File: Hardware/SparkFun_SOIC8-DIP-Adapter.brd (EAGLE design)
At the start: 20.3 x 20.3 mm, 17 parts, among them U1 GENERIC-SOIC8, U2 GENERIC-SOIC8, U3 GENERIC-SOIC8, U4 GENERIC-SOIC8

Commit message: Some small updates
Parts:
- FRAME1: value (none) -> frame
- JP1, JP2, JP3, JP4, JP5, JP6, JP7, JP8: value (none) -> 1x4
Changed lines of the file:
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@@
 <layer number="49" name="Reference" color="7" fill="1" visible="no" active="yes"/>
 <layer number="50" name="dxf" color="7" fill="1" visible="no" active="no"/>
-<layer number="51" name="tDocu" color="6" fill="1" visible="no" active="yes"/>
+<layer number="51" name="tDocu" color="6" fill="1" visible="yes" active="yes"/>
 <layer number="52" name="bDocu" color="7" fill="1" visible="no" active="yes"/>
 <layer number="53" name="tGND_GNDA" color="7" fill="9" visible="no" active="no"/>
@@
 <text x="19.558" y="-7.62" size="1.9304" layer="51" font="vector">Byron Jacquot</text>
 <text x="7.112" y="10.414" size="0.8128" layer="16" font="vector" ratio="25" rot="MR0">V11</text>
+<circle x="7.874" y="17.526" radius="0.127" width="0.254" layer="21"/>
+<circle x="18.034" y="17.526" radius="0.127" width="0.254" layer="21"/>
+<circle x="18.034" y="7.366" radius="0.127" width="0.254" layer="21"/>
+<circle x="7.874" y="7.366" radius="0.127" width="0.254" layer="21"/>
 </plain>
 <attributes>
@@
 </autorouter>
 <elements>
-<element name="FRAME1" library="SparkFun-Aesthetics" package="CREATIVE_COMMONS" value="" x="-11.43" y="-7.62">
+<element name="FRAME1" library="SparkFun-Aesthetics" package="CREATIVE_COMMONS" value="frame" x="-11.43" y="-7.62">
 <attribute name="VERSION" value="v01" x="-11.43" y="-7.62" size="1.778" layer="27" display="off"/>
 <attribute name="DESIGNER" value="NAME" x="-11.43" y="-7.62" size="1.778" layer="27" display="off"/>
 </element>
-<element name="JP1" library="SparkFun-Connectors" package="1X04_NO_SILK_ALL_ROUND" value="" x="1.27" y="19.05" rot="R270"/>
-<element name="JP2" library="SparkFun-Connectors" package="1X04_NO_SILK_ALL_ROUND" value="" x="8.89" y="19.05" rot="R270"/>
-<element name="JP3" library="SparkFun-Connectors" package="1X04_NO_SILK_ALL_ROUND" value="" x="11.43" y="19.05" rot="R270"/>
-<element name="JP4" library="SparkFun-Connectors" package="1X04_NO_SILK_ALL_ROUND" value="" x="19.05" y="19.05" rot="R270"/>
-<element name="JP5" library="SparkFun-Connectors" package="1X04_NO_SILK_ALL_ROUND" value="" x="1.27" y="8.89" rot="R270"/>
-<element name="JP6" library="SparkFun-Connectors" package="1X04_NO_SILK_ALL_ROUND" value="" x="8.89" y="8.89" rot="R270"/>
-<element name="JP7" library="SparkFun-Connectors" package="1X04_NO_SILK_ALL_ROUND" value="" x="11.43" y="8.89" rot="R270"/>
-<element name="JP8" library="SparkFun-Connectors" package="1X04_NO_SILK_ALL_ROUND" value="" x="19.05" y="8.89" rot="R270"/>
+<element name="JP1" library="SparkFun-Connectors" package="1X04_NO_SILK_ALL_ROUND" value="1x4" x="1.27" y="19.05" rot="R270"/>
+<element name="JP2" library="SparkFun-Connectors" package="1X04_NO_SILK_ALL_ROUND" value="1x4" x="8.89" y="19.05" rot="R270"/>
+<element name="JP3" library="SparkFun-Connectors" package="1X04_NO_SILK_ALL_ROUND" value="1x4" x="11.43" y="19.05" rot="R270"/>
+<element name="JP4" library="SparkFun-Connectors" package="1X04_NO_SILK_ALL_ROUND" value="1x4" x="19.05" y="19.05" rot="R270"/>
+<element name="JP5" library="SparkFun-Connectors" package="1X04_NO_SILK_ALL_ROUND" value="1x4" x="1.27" y="8.89" rot="R270"/>
+<element name="JP6" library="SparkFun-Connectors" package="1X04_NO_SILK_ALL_ROUND" value="1x4" x="8.89" y="8.89" rot="R270"/>
+<element name="JP7" library="SparkFun-Connectors" package="1X04_NO_SILK_ALL_ROUND" value="1x4" x="11.43" y="8.89" rot="R270"/>
+<element name="JP8" library="SparkFun-Connectors" package="1X04_NO_SILK_ALL_ROUND" value="1x4" x="19.05" y="8.89" rot="R270"/>
 <element name="U1" library="SparkFun-AnalogIC" package="SO08-UNIVERSAL" value="GENERIC-SOIC8" x="5.08" y="15.24" rot="R180"/>
 <element name="U2" library="SparkFun-AnalogIC" package="SO08-UNIVERSAL" value="GENERIC-SOIC8" x="15.24" y="15.24" rot="R180"/>
@@
 <polygon width="0.254" layer="16">
 <vertex x="7.62" y="11.684"/>
-<vertex x="7.62" y="10.668"/>
-<vertex x="4.572" y="10.668"/>
+<vertex x="7.62" y="11.176"/>
+<vertex x="4.572" y="11.176"/>
 <vertex x="4.572" y="11.684"/>
 </polygon>

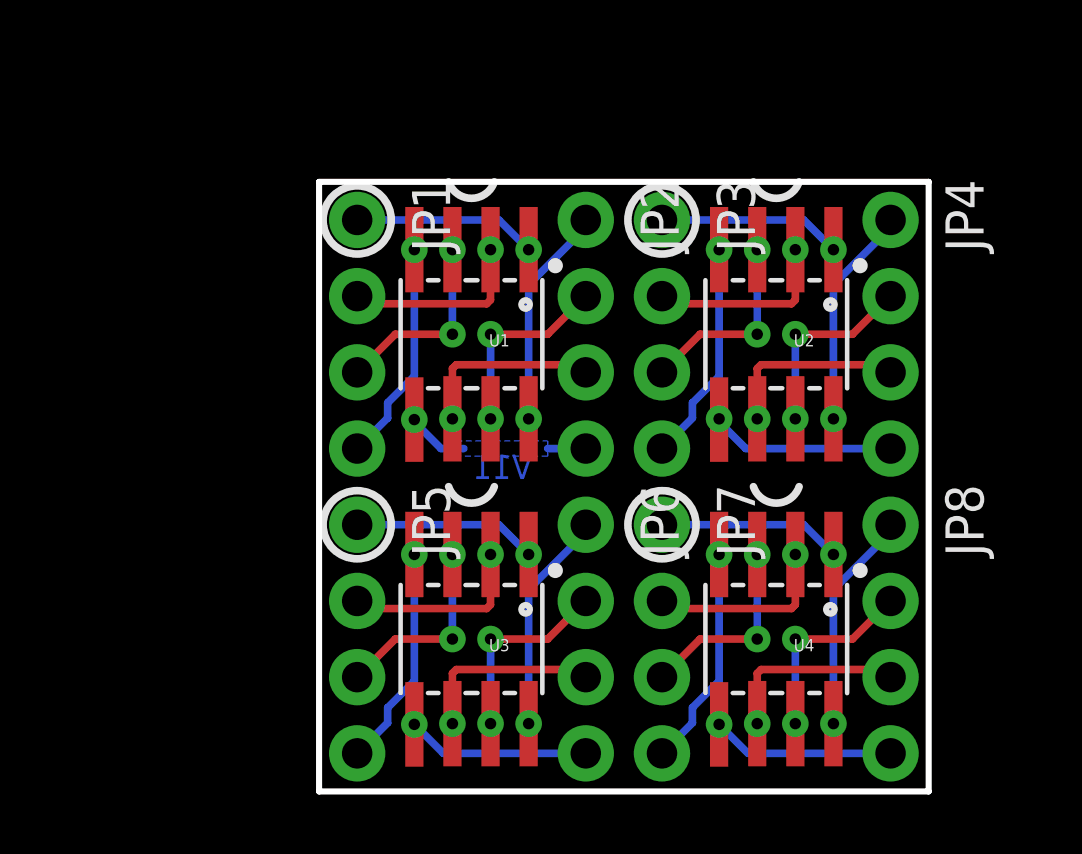
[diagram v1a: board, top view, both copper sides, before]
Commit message: Updated after group review.
-Fixed panelization.
-Added DIP pin numbers to bottom silk.
-Moved version # to top edge.
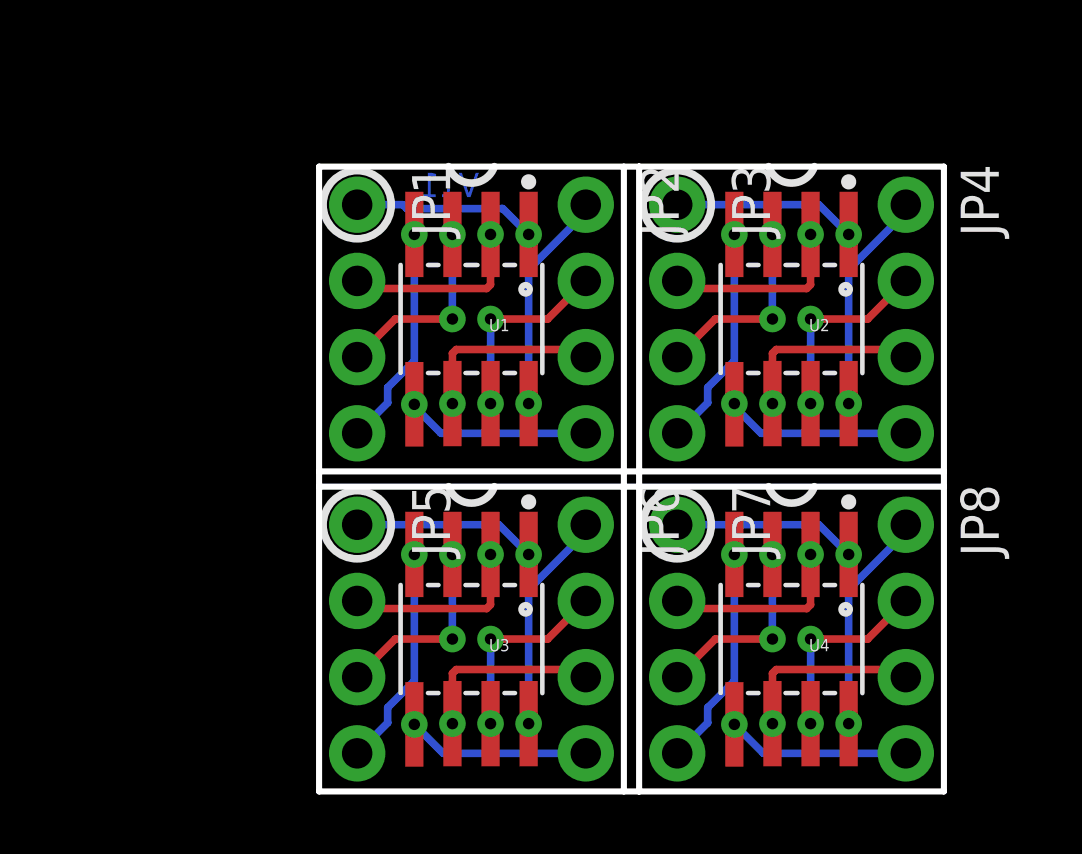
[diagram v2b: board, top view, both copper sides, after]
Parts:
- moved JP3 0.72 mm to (11.9, 19.6)
- moved LOGO1 0.72 mm to (18.3, 15.2)
- moved JP4 0.72 mm to (19.6, 19.6)
- moved U2 0.72 mm to (15.7, 15.7)
- moved JP7 0.51 mm to (11.9, 8.89)
- moved JP1 0.51 mm to (1.27, 19.6)
- moved JP2 0.51 mm to (8.89, 19.6)
- moved JP8 0.51 mm to (19.6, 8.89)
- moved LOGO2 0.51 mm to (5.08, 17.3)
- moved LOGO3 0.51 mm to (15.7, 6.35)
- moved U1 0.51 mm to (5.08, 15.7)
- moved U4 0.51 mm to (15.7, 5.08)
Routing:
- net N$8: track 3.37 -> 6.16 mm
- removed copper zone on layer 16, net N$8
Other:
- board size 20.3 x 20.3 mm -> 20.8 x 20.8 mm
- board text added: "1"
- board text added: "8"

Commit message: Updated with Pete's revised logos
To speed up CAM jobs.
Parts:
- LOGO4: device SparkFun-Aesthetics:SFE_LOGO_FLAME_.1 -> SparkFun-Aesthetics:SFE_LOGO_FLAME_.1@1
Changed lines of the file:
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@@
 <setting verticaltext="up"/>
 </settings>
-<grid distance="0.01" unitdist="inch" unit="inch" style="lines" multiple="1" display="yes" altdistance="0.001" altunitdist="inch" altunit="inch"/>
+<grid distance="0.05" unitdist="inch" unit="inch" style="lines" multiple="1" display="yes" altdistance="0.005" altunitdist="inch" altunit="inch"/>
 <layers>
 <layer number="1" name="Top" color="4" fill="1" visible="yes" active="yes"/>
@@
 <layer number="100" name="Muster" color="7" fill="1" visible="no" active="no"/>
 <layer number="101" name="Patch_Top" color="12" fill="4" visible="no" active="yes"/>
-<layer number="102" name="Vscore" color="7" fill="1" visible="yes" active="yes"/>
+<layer number="102" name="Vscore" color="7" fill="1" visible="no" active="yes"/>
 <layer number="103" name="tMap" color="7" fill="1" visible="no" active="yes"/>
 <layer number="104" name="Name" color="16" fill="1" visible="no" active="yes"/>
@@
 <element name="LOGO2" library="SparkFun-Aesthetics" package="OSHW-LOGO-S" value="OSHW-LOGOS" x="5.08" y="17.272" rot="MR0"/>
 <element name="LOGO3" library="SparkFun-Aesthetics" package="OSHW-LOGO-S" value="OSHW-LOGOS" x="15.748" y="6.35" rot="MR0"/>
-<element name="LOGO4" library="SparkFun-Aesthetics" package="SFE_LOGO_FLAME_.1" value="SFE_LOGO_FLAME.1_INCH" x="7.62" y="4.572" rot="MR0"/>
+<element name="LOGO4" library="SparkFun-Aesthetics" package="SFE_LOGO_FLAME_.1@1" value="SFE_LOGO_FLAME.1_INCH" x="7.62" y="4.572" rot="MR0"/>
 </elements>
 <signals>

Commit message: Checklist-related updates.
Should handle all issues:
-names/values were on wring layers
-added dimension lines
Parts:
- moved FRAME1 11.4 mm to (-16.5, -17.8)
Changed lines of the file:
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@@
 <layer number="45" name="Holes" color="7" fill="1" visible="yes" active="yes"/>
 <layer number="46" name="Milling" color="3" fill="1" visible="no" active="yes"/>
-<layer number="47" name="Measures" color="7" fill="1" visible="no" active="yes"/>
+<layer number="47" name="Measures" color="7" fill="1" visible="yes" active="yes"/>
 <layer number="48" name="Document" color="7" fill="1" visible="no" active="yes"/>
 <layer number="49" name="Reference" color="7" fill="1" visible="no" active="yes"/>
@@
 <text x="6.604" y="0.762" size="1.016" layer="22" font="vector" ratio="15" rot="MR0">DIP8</text>
 <text x="5.588" y="2.794" size="0.8128" layer="22" font="vector" ratio="15" rot="MR0">to</text>
-<text x="19.558" y="-7.62" size="1.9304" layer="51" font="vector">Byron Jacquot</text>
+<text x="15.748" y="-17.78" size="1.9304" layer="51" font="vector">Byron Jacquot</text>
 <text x="5.334" y="19.812" size="0.8128" layer="16" font="vector" ratio="25" rot="MR0">V11</text>
 <circle x="6.985" y="20.32" radius="0.127" width="0.254" layer="21"/>
@@
 <wire x1="10.668" y1="20.828" x2="10.668" y2="0" width="0.2032" layer="20"/>
 <wire x1="0" y1="10.668" x2="20.828" y2="10.668" width="0.2032" layer="20"/>
+<dimension x1="0" y1="0" x2="0" y2="20.828" x3="-11.557" y3="10.414" textsize="1.27" textratio="15" layer="47" unit="inch" visible="yes"/>
+<dimension x1="0" y1="0" x2="0" y2="10.16" x3="-5.08" y3="5.08" textsize="1.27" textratio="15" layer="47" unit="inch" visible="yes"/>
+<dimension x1="0" y1="0" x2="20.828" y2="0" x3="10.414" y3="-8.89" textsize="1.27" textratio="15" layer="47" unit="inch" visible="yes"/>
+<dimension x1="0" y1="0" x2="10.16" y2="0" x3="5.08" y3="-3.81" textsize="1.27" textratio="15" layer="47" unit="inch" visible="yes"/>
 </plain>
 <attributes>
@@
 </autorouter>
 <elements>
-<element name="FRAME1" library="SparkFun-Aesthetics" package="CREATIVE_COMMONS" value="frame" x="-11.43" y="-7.62">
-<attribute name="VERSION" value="v01" x="-11.43" y="-7.62" size="1.778" layer="27" display="off"/>
-<attribute name="DESIGNER" value="NAME" x="-11.43" y="-7.62" size="1.778" layer="27" display="off"/>
+<element name="FRAME1" library="SparkFun-Aesthetics" package="CREATIVE_COMMONS" value="frame" x="-16.51" y="-17.78">
+<attribute name="VERSION" value="v01" x="-16.51" y="-17.78" size="1.778" layer="27" display="off"/>
+<attribute name="DESIGNER" value="NAME" x="-16.51" y="-17.78" size="1.778" layer="27" display="off"/>
 </element>
 <element name="JP1" library="SparkFun-Connectors" package="1X04_NO_SILK_ALL_ROUND" value="1x4" x="1.27" y="19.558" rot="R270"/>

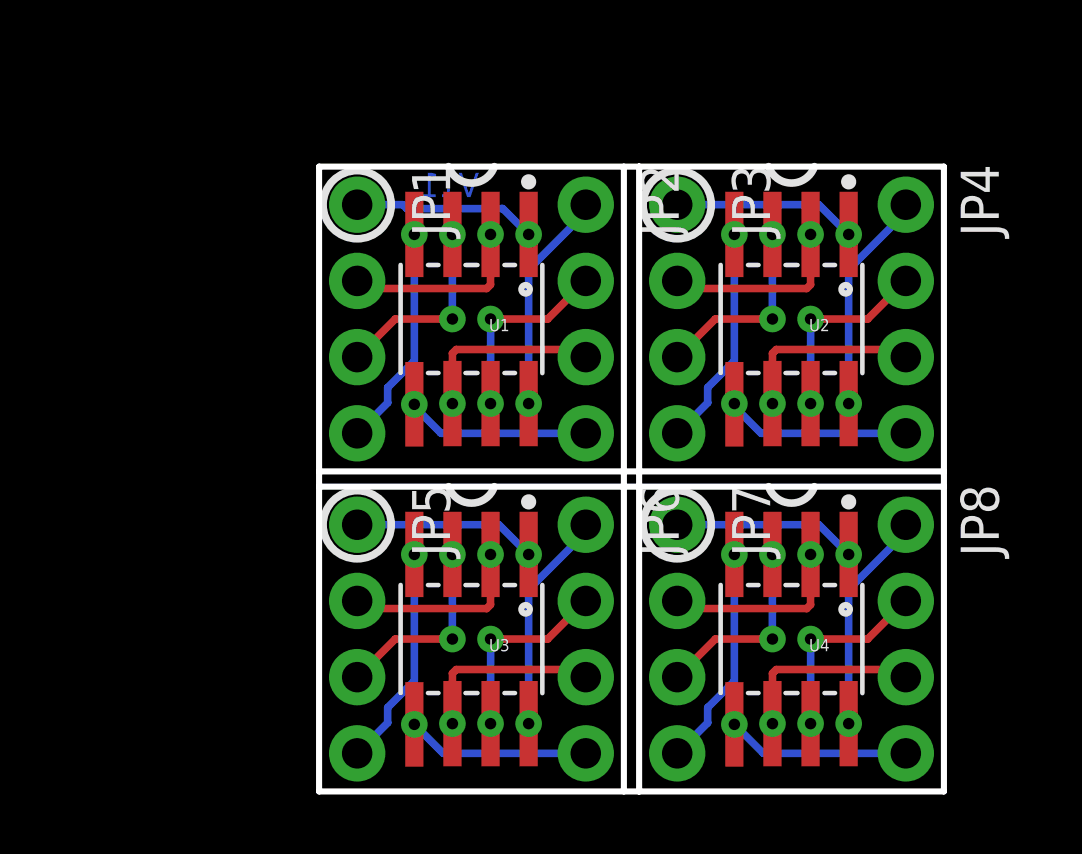
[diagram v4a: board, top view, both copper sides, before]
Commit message: Updates after reviewing protos.
Wider SOIC footprint.
DIP pin 1 marked with square pad.
Some rearrangement of silk elements.
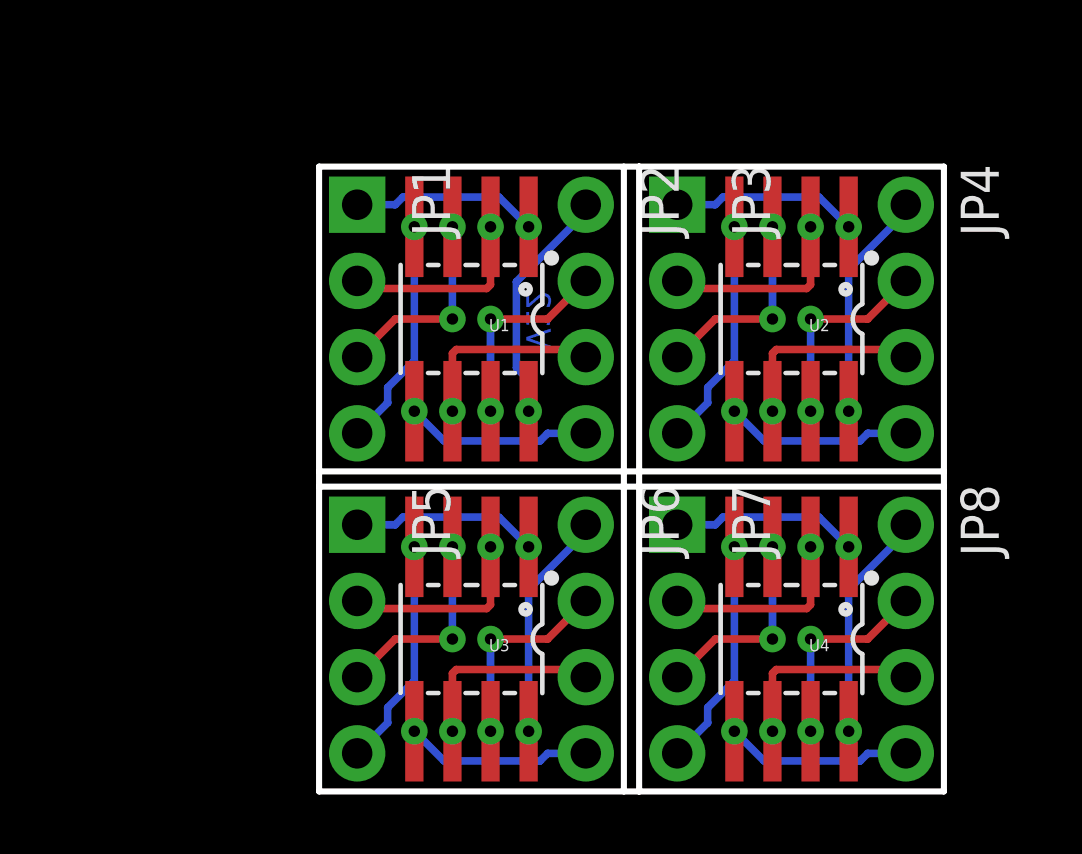
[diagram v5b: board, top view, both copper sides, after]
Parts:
- JP1, JP3, JP5, JP7: device SparkFun-Connectors:1X04_NO_SILK_ALL_ROUND -> SparkFun-Connectors:1X04_NO_SILK
- moved FRAME1 7.73 mm to (-15.2, -10.2)
- moved LOGO3 0.25 mm to (15.7, 6.60)
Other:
- board text added: "V12"
- board text removed: "V11"

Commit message: Fixing review issues
* CC block location.
* Ver # mismatch between schem and PCB.
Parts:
- moved FRAME1 7.62 mm to (-15.2, -17.8)
